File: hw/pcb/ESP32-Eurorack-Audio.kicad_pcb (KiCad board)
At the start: 2 copper layers, 40.6 x 99.1 mm, 131 parts, among them J301 USB_B_Micro, J401 PWR, J501 AUEXT, J502 RIN, J503 LIN, J504 ROUT, J505 LOUT, J601 CV0IN, J602 TRG0, J603 CV1IN, J604 TRG1, Q301 SS8050-G, Q302 SS8050-G, Q601 SS8050, Q602 SS8050, SW601 SW_Push_Dual, SW602 SW_Push_Dual, U201 MIC803, U202 ESP32-WROVER, U301 CP2102N-A01-GQFN28, U401 R-78E3.3-1.0, U402 ADP7118, U501 WM8731, U502 TL072, U503 TL072, U601 MCP6002-xSN, Y501 11.289600

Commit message: wm8978 PCB design files
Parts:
- removed C521: 10u, Capacitor_SMD:C_0402_1005Metric
- removed J501: AUEXT, Connector_PinHeader_2.54mm:PinHeader_2x05_P2.54mm_Vertical_SMD
- removed Y501: 11.289600, Crystal:Crystal_SMD_3225-4Pin_3.2x2.5mm
- added JP505: ROUT, Jumper:SolderJumper-3_P1.3mm_Open_RoundedPad1.0x1.5mm_NumberLabels, F.Cu at (104.3, 93.5)
- added JP506: LOUT, Jumper:SolderJumper-3_P1.3mm_Open_RoundedPad1.0x1.5mm_NumberLabels, F.Cu at (104.4, 97.3)
- added JP507: LIN, Jumper:SolderJumper-3_P1.3mm_Open_RoundedPad1.0x1.5mm_NumberLabels, F.Cu at (110.5, 97.3)
- added JP508: RIN, Jumper:SolderJumper-3_P1.3mm_Open_RoundedPad1.0x1.5mm_NumberLabels, F.Cu at (110.5, 93.5)
- added L501: 10uH, Capacitor_SMD:C_0603_1608Metric, B.Cu at (97.8, 85.5)
- C502, C514, C520: value 10u -> 100n
- C503, C508: value 100n -> 4.7u
- C505, C506: value 18p -> 4.7u
- C507: value 10u -> 4.7u
- U501: value WM8731 -> WM8978CGEFL_V; footprint Package_SO:SSOP-28_5.3x10.2mm_P0.65mm -> Package_DFN_QFN:QFN-32-1EP_5x5mm_P0.5mm_EP3.65x3.65mm_ThermalVias
- moved C506 16.1 mm to (108.6, 91.7), turned to 270 degrees
- moved C502 13.7 mm to (99.8, 86.3), turned to 0 degrees
- moved C508 13.3 mm to (112.5, 87.3), turned to 0 degrees
- moved C503 12.5 mm to (101.8, 88.5), turned to 180 degrees
- moved C520 11.6 mm to (101.8, 86.3), turned to 180 degrees
- moved C505 6.93 mm to (101.8, 85.2), turned to 180 degrees
- moved C515 5.69 mm to (101.8, 89.6), turned to 180 degrees
- moved C507 4.76 mm to (101.8, 87.3), turned to 180 degrees
- moved C523 4.38 mm to (109.6, 91.7), turned to 270 degrees
- moved C522 4.32 mm to (112.5, 88.3), turned to 0 degrees
- moved U501 1.66 mm to (107.3, 86.5), turned to 270 degrees
- moved C514 1.28 mm to (101.8, 84.2), turned to 180 degrees
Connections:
- C502 pad 1: +3.3VA -> +3.3VP
- C505 pad 1: Net-(C505-Pad1) -> +3.3VA
- C506 pad 1: Net-(C506-Pad1) -> +3.3VP
- C508 pad 1: /CODEC/VMID -> +3.3VP
- C520 pad 1: +3.3VA -> /CODEC/VMID
- C522 pad 1: +3.3VA -> +3.3VP
- C523 pad 1: +3.3VA -> +3.3VP
- U501 pad 1: +3.3VA -> (no net)
- U501 pad 10: /CODEC/RHPOUT -> /CODEC/DACDAT
- U501 pad 11: GND -> /ESP-main/IO0
- U501 pad 12: /CODEC/LOUT -> GND
- U501 pad 13: /CODEC/ROUT -> +3.3VP
- U501 pad 14: +3.3VA -> +3.3VP
- U501 pad 15: GND -> /ESP-main/IO4
- U501 pad 16: /CODEC/VMID -> /ESP-main/IO12
- U501 pad 17: /CODEC/MICBIAS -> /ESP-main/IO13
- U501 pad 18: /CODEC/MICIN -> +3.3VP
- U501 pad 19: /CODEC/RIN -> Net-(JP507-Pad1)
- U501 pad 20: /CODEC/LIN -> Net-(JP508-Pad1)
- U501 pad 21: +3.3VA -> Net-(JP505-Pad1)
- U501 pad 22: /ESP-main/IO4 -> Net-(JP506-Pad1)
- U501 pad 23: /ESP-main/IO13 -> (no net)
- U501 pad 24: /ESP-main/IO12 -> GND
- U501 pad 25: Net-(C505-Pad1) -> (no net)
- U501 pad 26: Net-(C506-Pad1) -> +3.3VA
- U501 pad 27: +3.3VA -> /CODEC/VMID
- U501 pad 3: /CODEC/BCLK -> /CODEC/L2
- U501 pad 4: /CODEC/DACDAT -> (no net)
- U501 pad 5: /ESP-main/IO19 -> (no net)
- U501 pad 6: /CODEC/ADCDAT -> /CODEC/R2
- U501 pad 8: +3.3VA -> /CODEC/BCLK
- U501 pad 9: /CODEC/LHPOUT -> /CODEC/ADCDAT
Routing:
- net /ESP-main/IO0: track 3.61 -> 45.1 mm, vias 1 -> 2
- net +3.3VP: track 0.00 -> 35.0 mm, vias 0 -> 2
- net /CODEC/LIN: track 37.8 -> 10.4 mm, vias 3 -> 1
- net Net-(JP506-Pad3): track 0.00 -> 25.6 mm, vias 0 -> 1
- net +3.3VA: track 55.1 -> 30.7 mm, vias 5 -> 2
- net /CODEC/L2: track 0.00 -> 18.3 mm, vias 0 -> 1
- net /CODEC/LOUT: track 13.5 -> 31.3 mm, vias 2 -> 1
- net /CODEC/R2: track 0.00 -> 14.0 mm, vias 0 -> 1
- net /ESP-main/IO12: track 53.4 -> 41.3 mm
- net Net-(C505-Pad1): track 12.0 -> 0.00 mm, vias 2 -> 0
- net Net-(C506-Pad1): track 11.7 -> 0.00 mm, vias 2 -> 0
- net Net-(JP507-Pad1): track 0.00 -> 11.3 mm, vias 0 -> 1
- net Net-(JP505-Pad3): track 0.00 -> 10.5 mm, vias 0 -> 1
- net /CODEC/ROUT: track 21.4 -> 12.3 mm, vias 3 -> 2
- net Net-(JP506-Pad1): track 0.00 -> 9.01 mm, vias 0 -> 1
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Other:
- board text added: "esp32-eurorack-tbd (c) 2020 R. Manzke Rev-C"
- board text removed: "esp32-eurorack-tbd (c) 2019 R. Manzke Rev-B"

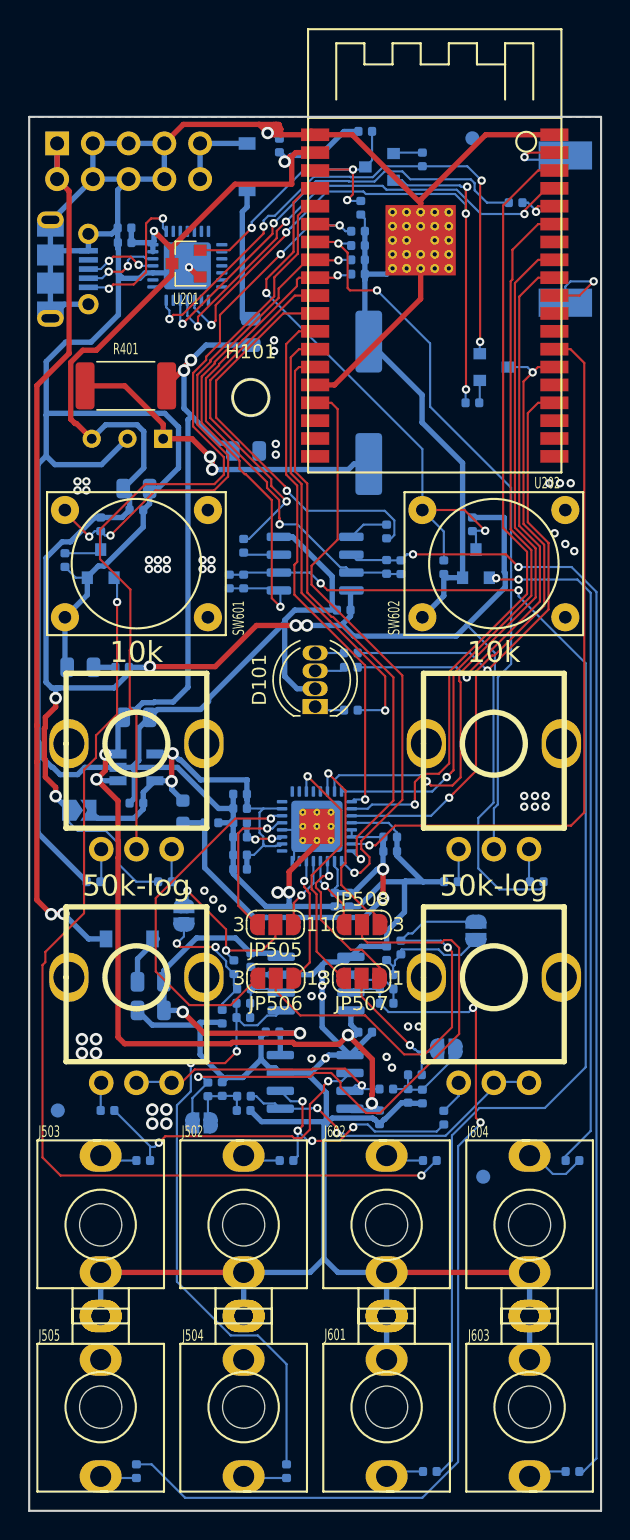
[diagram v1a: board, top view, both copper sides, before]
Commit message: fixed severe PCB issue, clearance of ground fills was too small, could lead to thermal instability
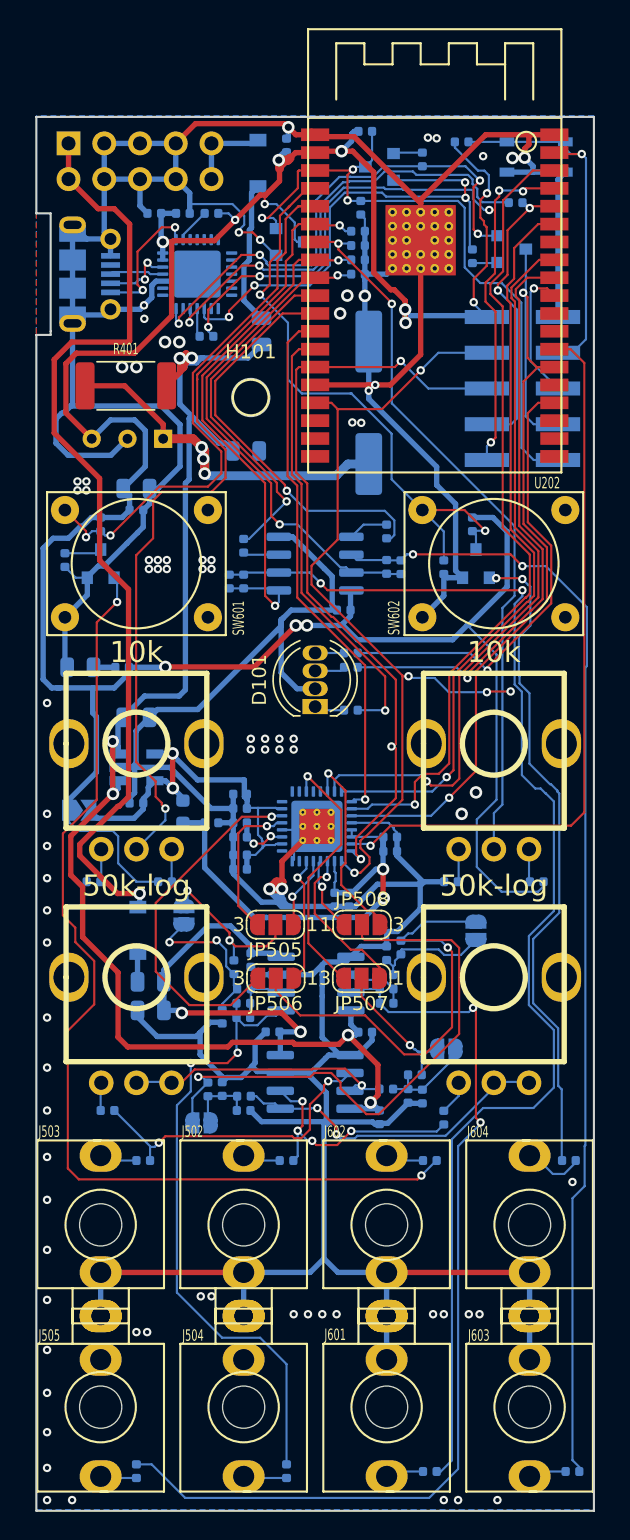
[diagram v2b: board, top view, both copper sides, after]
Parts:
- removed FID101, FID102, FID103: Fiducial, Fiducial:Fiducial_1mm_Mask2mm
- removed TP101, TP102: ~, TestPoint:TestPoint_Keystone_5019_Minature
- added J101: EXT, Connector_PinHeader_2.54mm:PinHeader_2x05_P2.54mm_Vertical_SMD, B.Cu at (121.9, 55.4)
- added R104: 10k, Resistor_SMD:R_0402_1005Metric, B.Cu at (117.6, 37.9)
- added R304: 4k7, Resistor_SMD:R_0402_1005Metric, B.Cu at (99.8, 42.9)
- added R305: 470R, Resistor_SMD:R_0402_1005Metric, B.Cu at (99.4, 51.7)
- added SW101: CAL, switches:PTS810, B.Cu at (125.0, 37.9)
- U201: moved to B.Cu
- moved R303 10.4 mm to (118.3, 46.0), turned to 90 degrees
- moved Q302 8.48 mm to (121.1, 45.5)
- moved U201 7.55 mm to (105.4, 45.0), turned to 0 degrees
- moved C301 4.63 mm to (97.8, 42.9), turned to 0 degrees
- moved C302 2.36 mm to (95.7, 42.9)
- moved J301 1.62 mm to (91.2, 47.3)
- moved U301 0.91 mm to (98.8, 47.3)
- moved D402 0.86 mm to (94.6, 93.9), turned to 270 degrees
- moved J401 0.81 mm to (89.6, 38.0)
- moved D401 0.81 mm to (103.1, 39.4)
- moved L401 0.77 mm to (103.4, 51.3)
- moved C201 0.51 mm to (105.1, 38.1)
- moved R609 0.25 mm to (125.2, 110.3)
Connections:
- net /ESP-main/EN renamed /EN
- net /ESP-main/IO0 renamed /IO0
- net /ESP-main/IO12 renamed /SCLK
- net /ESP-main/IO13 renamed /MOSI
- net /ESP-main/RXD renamed /RXD
- U202 pad 29: /ESP-main/IO5 -> /EXCS
- U202 pad 35: /ESP-main/TXD -> /TXD
- U202 pad 37: /ESP-main/IO23 -> /RST
- U301 pad 25: /ESP-main/TXD -> Net-(R305-Pad2)
- U301 pad 9: (no net) -> Net-(R304-Pad1)
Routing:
- net /TXD: track 0.00 -> 53.6 mm, vias 0 -> 6
- net +3V3: track 164.5 -> 209.2 mm, vias 7 -> 12
- net /ESP-main/TXD: track 34.1 -> 0.00 mm, vias 3 -> 0
- net /RST: track 0.00 -> 26.4 mm, vias 0 -> 1
- net /EN: track 23.4 -> 47.6 mm
- net /MOSI: track 41.6 -> 62.3 mm, vias 1 -> 5
- net /IO0: track 45.1 -> 64.7 mm
- net GND: track 453.3 -> 434.9 mm, vias 55 -> 82
- net /RXD: track 2.89 -> 21.2 mm, vias 1 -> 2
- net /SCLK: track 41.3 -> 54.9 mm, vias 1 -> 3
- net /USB/RTS: track 48.9 -> 35.9 mm, vias 5 -> 4
- net +12V: track 94.5 -> 105.3 mm
- net /EXCS: track 0.00 -> 9.68 mm, vias 0 -> 1
- net /ESP-main/IO5: track 6.53 -> 0.00 mm, vias 1 -> 0
- net /ESP-main/IO23: track 5.23 -> 0.00 mm, vias 1 -> 0
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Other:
- board size 40.6 x 99.1 mm -> 39.6 x 99.1 mm
- net class Power added: clearance 0.254, trace_width 0.254, via_dia 0.889, via_drill 0.508
- board text added: "RST"
- board text added: "esp32-eurorack-tbd (c) 2020 R. Manzke Rev-G (like in GOOD)"
- board text removed: "esp32-eurorack-tbd (c) 2020 R. Manzke Rev-C"

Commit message: Updated Eurorack hw to Rev. H
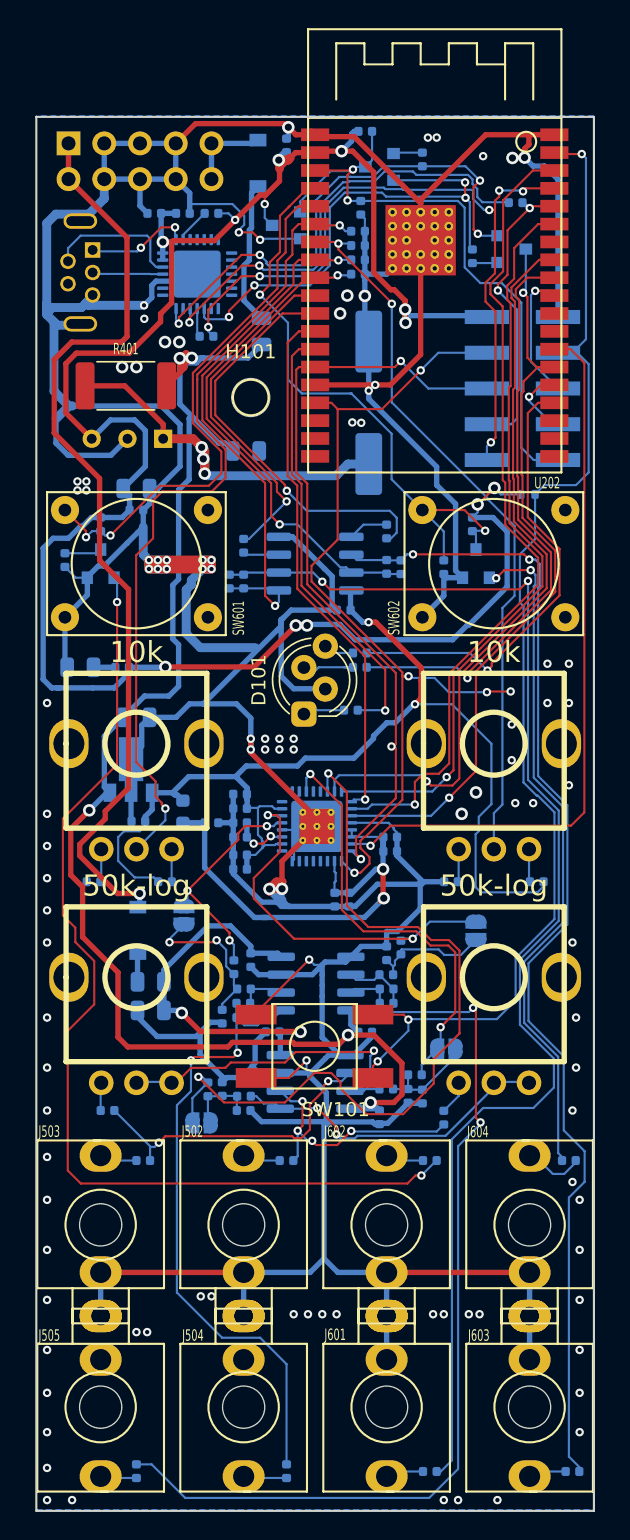
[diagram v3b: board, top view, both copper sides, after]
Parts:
- removed JP401: Jumper_2_Open, Jumper:SolderJumper-2_P1.3mm_Open_TrianglePad1.0x1.5mm
- removed JP505: ROUT, Jumper:SolderJumper-3_P1.3mm_Open_RoundedPad1.0x1.5mm_NumberLabels
- removed JP506: LOUT, Jumper:SolderJumper-3_P1.3mm_Open_RoundedPad1.0x1.5mm_NumberLabels
- removed JP507: LIN, Jumper:SolderJumper-3_P1.3mm_Open_RoundedPad1.0x1.5mm_NumberLabels
- removed JP508: RIN, Jumper:SolderJumper-3_P1.3mm_Open_RoundedPad1.0x1.5mm_NumberLabels
- D101: footprint LED_THT:LED_D5.0mm-4_RGB -> LED_THT:LED_D5.0mm-4_RGB_Staggered_Pins
- J301: value USB_B_Micro -> USB_B_Mini; footprint Connector_USB:USB_Micro-B_Molex-105017-0001 -> Connector_USB:USB_Mini-B_Tensility_54-00023_Vertical
- SW101: value CAL -> PUSHBTN; footprint switches:PTS810 -> switches:TactilePB_6x6; moved to F.Cu
- U201: value MIC803 -> CN61C
- U402: value ADP7118 -> LD2981ABU33TR; footprint Package_TO_SOT_SMD:TSOT-23-5 -> Package_TO_SOT_SMD:SOT-89-3
- moved SW101 66.7 mm to (107.1, 102.1)
- moved R104 25.5 mm to (122.3, 62.9)
- moved J301 1.73 mm to (91.4, 45.5), turned to 270 degrees
- moved C407 1.30 mm to (94.6, 86.2)
- moved U201 1.21 mm to (105.1, 43.8), turned to 180 degrees
- moved D101 0.96 mm to (106.4, 78.5)
- moved R102 0.64 mm to (110.3, 74.2)
- moved R103 0.64 mm to (110.3, 75.2)
- moved U402 0.41 mm to (94.1, 82.5), turned to 90 degrees
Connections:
- net /EXCS renamed /IO5
- C607 pad 1: +3V3 -> +3.3VA
- J101 pad 3: /RST -> /IO23
- J101 pad 7: /IO0 -> /IO2
- J301 pad 4: (no net) -> Net-(J301-Pad4)
- J504 pad 2: (no net) -> Net-(J504-Pad2)
- J505 pad 2: (no net) -> Net-(J505-Pad2)
- R104 pad 2: /RST -> /IO23
- R611 pad 1: +3V3 -> +3.3VA
- R612 pad 1: +3V3 -> +3.3VA
- SW101 pad 1: /RST -> /IO23
- SW101 pad 2: /RST -> GND
- SW101 pad 3: GND -> /IO23
- SW601 pad 2: (no net) -> Net-(SW601-Pad2)
- SW601 pad 4: (no net) -> Net-(SW601-Pad4)
- SW602 pad 2: (no net) -> Net-(SW602-Pad2)
- SW602 pad 4: (no net) -> Net-(SW602-Pad4)
- U201 pad 1: GND -> /EN
- U201 pad 2: /EN -> GND
- U202 pad 17: (no net) -> Net-(U202-Pad17)
- U202 pad 18: (no net) -> Net-(U202-Pad18)
- U202 pad 19: (no net) -> Net-(U202-Pad19)
- U202 pad 20: (no net) -> Net-(U202-Pad20)
- U202 pad 21: (no net) -> Net-(U202-Pad21)
- U202 pad 22: (no net) -> Net-(U202-Pad22)
- U202 pad 24: (no net) -> /IO2
- U202 pad 27: (no net) -> Net-(U202-Pad27)
- U202 pad 28: (no net) -> Net-(U202-Pad28)
- U202 pad 32: (no net) -> Net-(U202-Pad32)
- U202 pad 37: /RST -> /IO23
- U301 pad 1: (no net) -> Net-(U301-Pad1)
- U301 pad 10: (no net) -> Net-(U301-Pad10)
- U301 pad 11: (no net) -> Net-(U301-Pad11)
- U301 pad 12: (no net) -> Net-(U301-Pad12)
- U301 pad 13: (no net) -> Net-(U301-Pad13)
- U301 pad 14: (no net) -> Net-(U301-Pad14)
- U301 pad 15: (no net) -> Net-(U301-Pad15)
- U301 pad 16: (no net) -> Net-(U301-Pad16)
- U301 pad 17: (no net) -> Net-(U301-Pad17)
- U301 pad 18: (no net) -> Net-(U301-Pad18)
- U301 pad 19: (no net) -> Net-(U301-Pad19)
- U301 pad 2: (no net) -> Net-(U301-Pad2)
- U301 pad 20: (no net) -> Net-(U301-Pad20)
- U301 pad 21: (no net) -> Net-(U301-Pad21)
- U301 pad 22: (no net) -> Net-(U301-Pad22)
- U301 pad 23: (no net) -> Net-(U301-Pad23)
- U301 pad 27: (no net) -> Net-(U301-Pad27)
- U402 pad 1: +12V -> +3.3VA
- U501 pad 1: (no net) -> Net-(U501-Pad1)
- U501 pad 2: (no net) -> Net-(U501-Pad2)
- U501 pad 23: (no net) -> Net-(U501-Pad23)
- U501 pad 25: (no net) -> Net-(U501-Pad25)
- U501 pad 29: Net-(JP505-Pad3) -> /CODEC/ROUT
- U501 pad 3: /CODEC/L2 -> /CODEC/LIN
- U501 pad 30: Net-(JP506-Pad3) -> /CODEC/LOUT
- U501 pad 32: (no net) -> Net-(U501-Pad32)
- U501 pad 4: (no net) -> Net-(U501-Pad4)
- U501 pad 5: (no net) -> Net-(U501-Pad5)
- U501 pad 6: /CODEC/R2 -> /CODEC/RIN
- U601 pad 8: +3V3 -> +3.3VA
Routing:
- net /IO23: track 0.00 -> 87.0 mm, vias 0 -> 3
- net +3V3: track 209.2 -> 149.1 mm
- net GND: track 434.9 -> 488.4 mm, vias 82 -> 103
- net +3.3VA: track 30.9 -> 78.5 mm
- net /RST: track 26.4 -> 0.00 mm, vias 1 -> 0
- net Net-(JP506-Pad3): track 25.4 -> 0.00 mm, vias 1 -> 0
- net /CODEC/LIN: track 10.4 -> 31.2 mm, vias 1 -> 2
- net /CODEC/L2: track 18.5 -> 0.00 mm, vias 1 -> 0
- net /CODEC/RIN: track 40.9 -> 55.7 mm, vias 1 -> 2
- net /CODEC/R2: track 14.0 -> 0.00 mm, vias 1 -> 0
- net Net-(U501-Pad19): track 11.3 -> 0.00 mm, vias 1 -> 0
- net /IO0: track 64.7 -> 53.9 mm
- net Net-(JP505-Pad3): track 10.5 -> 0.00 mm, vias 1 -> 0
- net Net-(U501-Pad22): track 9.07 -> 0.00 mm, vias 1 -> 0
- net Net-(U501-Pad20): track 5.54 -> 0.00 mm, vias 1 -> 0
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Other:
- outline, holes or cut-outs redrawn
- board text added: "esp32-eurorack-tbd (c) 2021 R. Manzke Rev-H"
- board text removed: "RST"
- board text removed: "esp32-eurorack-tbd (c) 2020 R. Manzke Rev-G (like in GOOD)"
